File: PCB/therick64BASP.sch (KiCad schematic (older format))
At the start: 165 parts, among them J1 TYPE-C-31-M12_13, J2 AVR-ISP-6, K1 KEYSW, K10 KEYSW, K11 KEYSW, K12 KEYSW, K13 KEYSW, K14 KEYSW, K15 KEYSW, K16 KEYSW, K17 KEYSW, K18 KEYSW, K19 KEYSW, K2 KEYSW, K20 KEYSW, K21 KEYSW, K22 KEYSW, K23 KEYSW, K24 KEYSW, K25 KEYSW, K26 KEYSW, K27 KEYSW, K28 KEYSW, K29 KEYSW, K3 KEYSW, K30 KEYSW, K31 KEYSW, K32 KEYSW, K33 KEYSW, K34 KEYSW, K35 KEYSW, K36 KEYSW, K37 KEYSW, K38 KEYSW, K39 KEYSW, K4 KEYSW, K40 KEYSW, K41 KEYSW, K42 KEYSW, K43 KEYSW, K44 KEYSW, K45 KEYSW, K46 KEYSW, K47 KEYSW, K48 KEYSW, K49 KEYSW, K5 KEYSW, K50 KEYSW, K51 KEYSW, K52 KEYSW, K53 KEYSW, K54 KEYSW, K55 KEYSW, K56 KEYSW, K57 KEYSW, K58 KEYSW, K59 KEYSW, K6 KEYSW, K60 KEYSW, K61 KEYSW, K62 KEYSW, K63 KEYSW, K64 KEYSW, K7 KEYSW, K8 KEYSW, K9 KEYSW, SW1 SW_PUSH, U1 ATMEGA32U4, U2 HOLE, U3 USBLC6-2SC6, U4 HOLE, U5 HOLE, U6 HOLE, U7 HOLE, U8 HOLE, Y1 16MHz

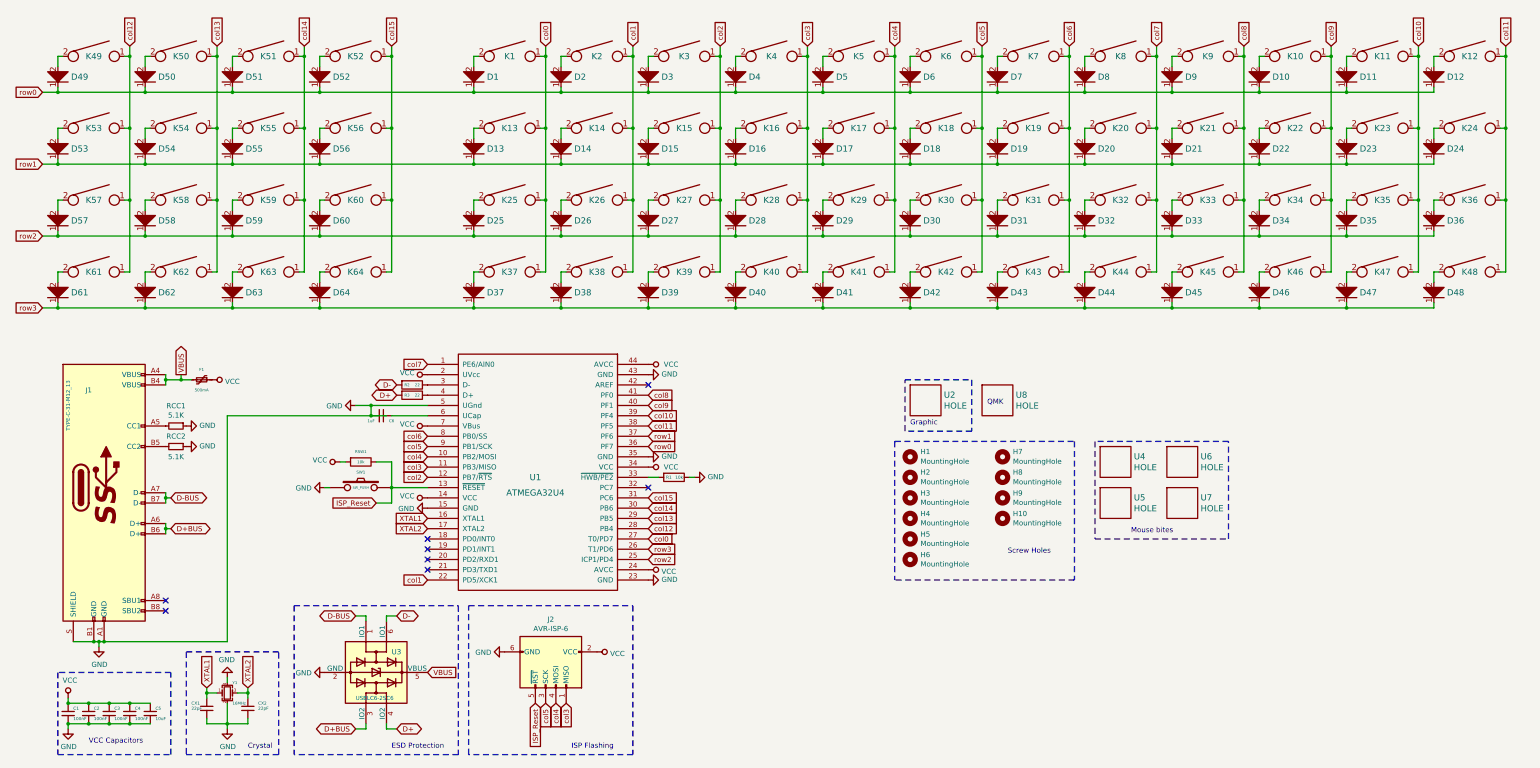
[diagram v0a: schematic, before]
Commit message: Changed pins to make routing cleaner
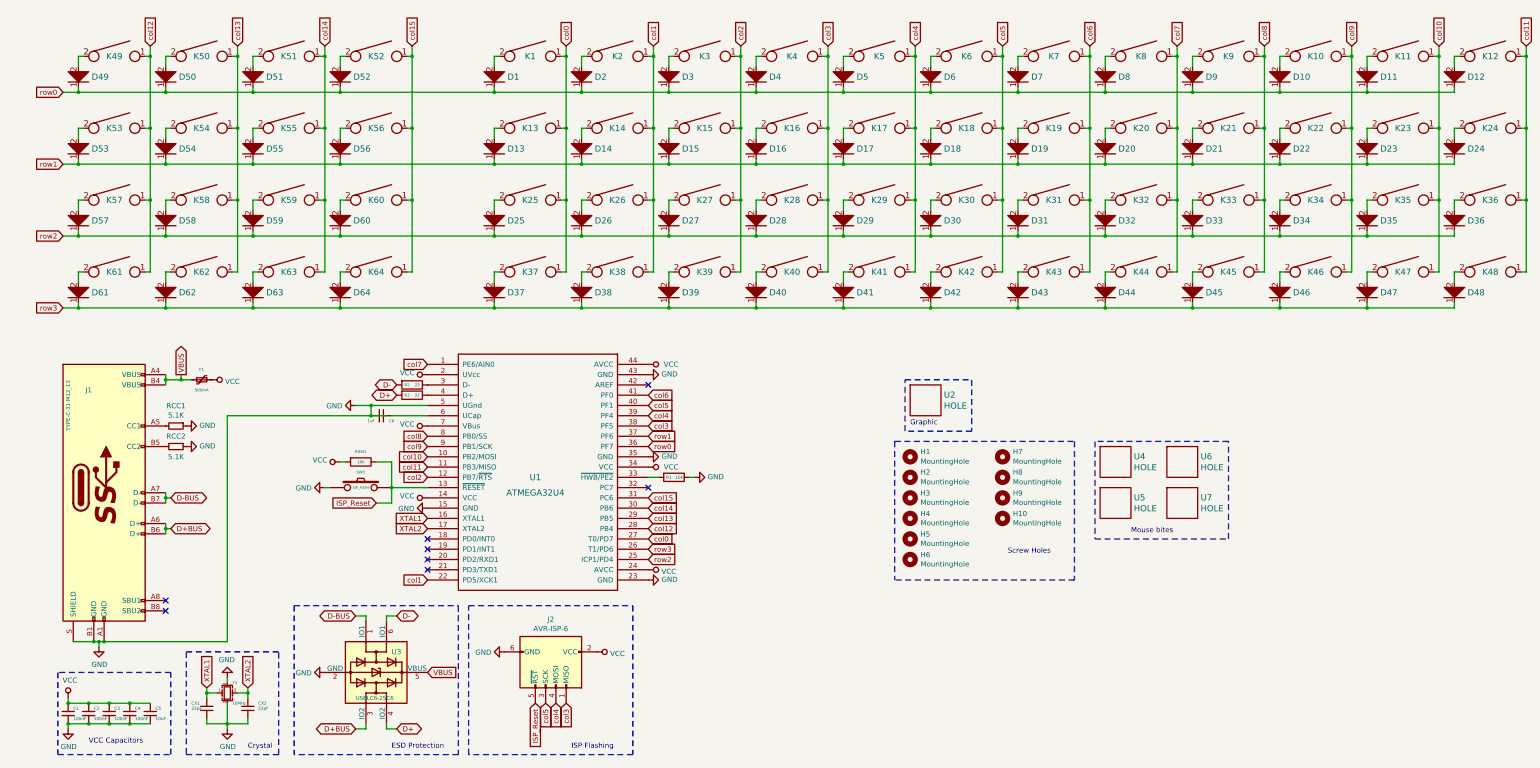
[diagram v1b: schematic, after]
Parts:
- removed U8: HOLE, Artwork:QMKBadgeSmall, symbol lets_split-cache:HOLE
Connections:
- net col10: now also U1.10 (PB2/MOSI); no longer U1.39 (PF4)
- net col11: now also U1.11 (PB3/MISO); no longer U1.38 (PF5)
- net col3: now also U1.38 (PF5); no longer U1.11 (PB3/MISO)
- net col4: now also U1.39 (PF4); no longer U1.10 (PB2/MOSI)
- net col5: now also U1.40 (PF1); no longer U1.9 (PB1/SCK)
- net col6: now also U1.41 (PF0); no longer U1.8 (PB0/SS)
- net col8: now also U1.8 (PB0/SS); no longer U1.41 (PF0)
- net col9: now also U1.9 (PB1/SCK); no longer U1.40 (PF1)
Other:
- note removed: "QMK"
- moved on the sheet: D1, D10, D11, D12, D13, D14, D15, D16, D17, D18, D19, D2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

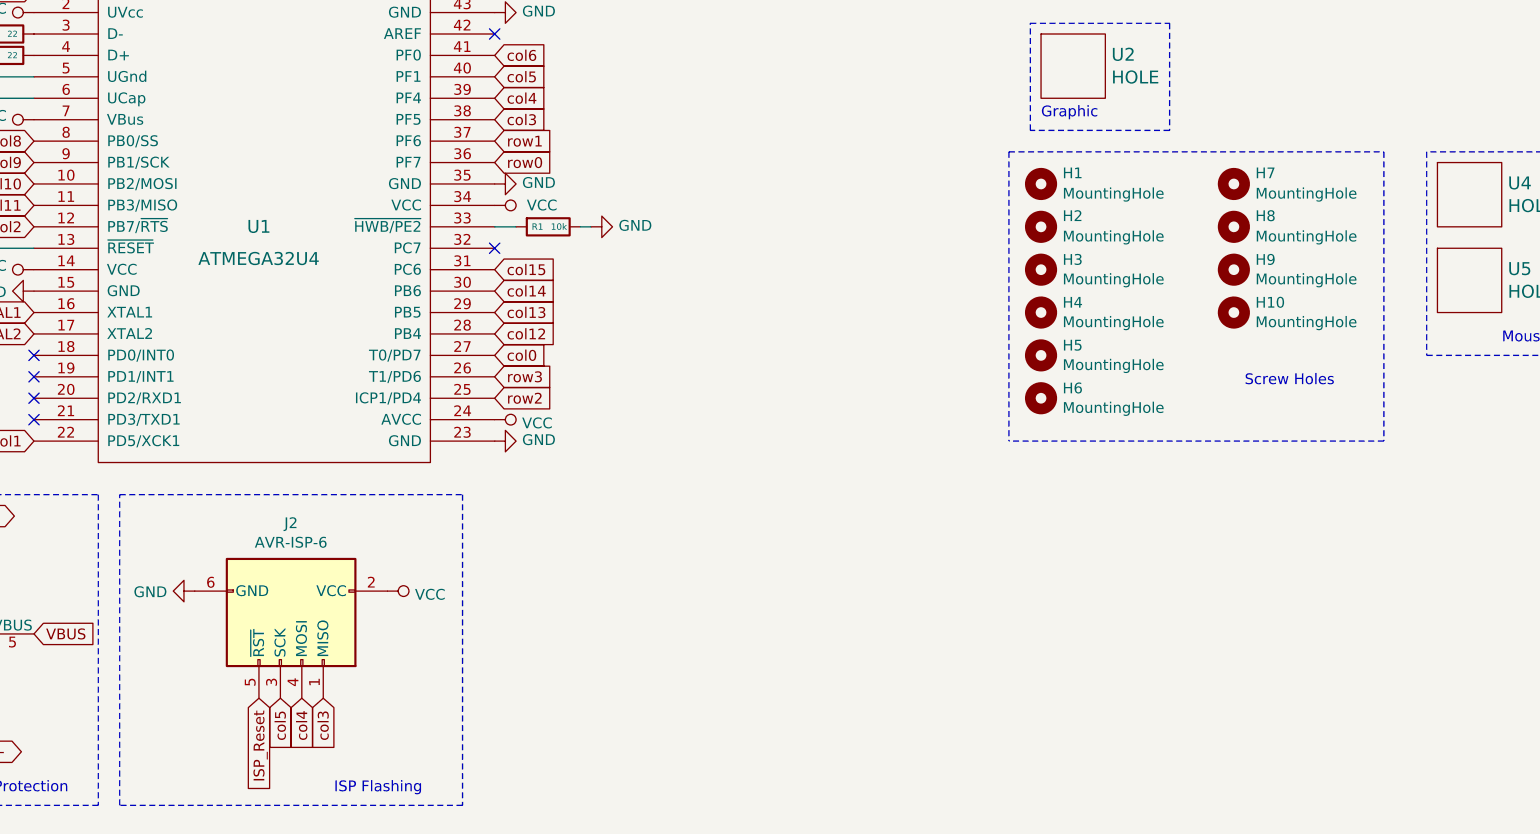
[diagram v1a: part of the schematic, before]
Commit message: Remapped ISP Flash, added mounting holes
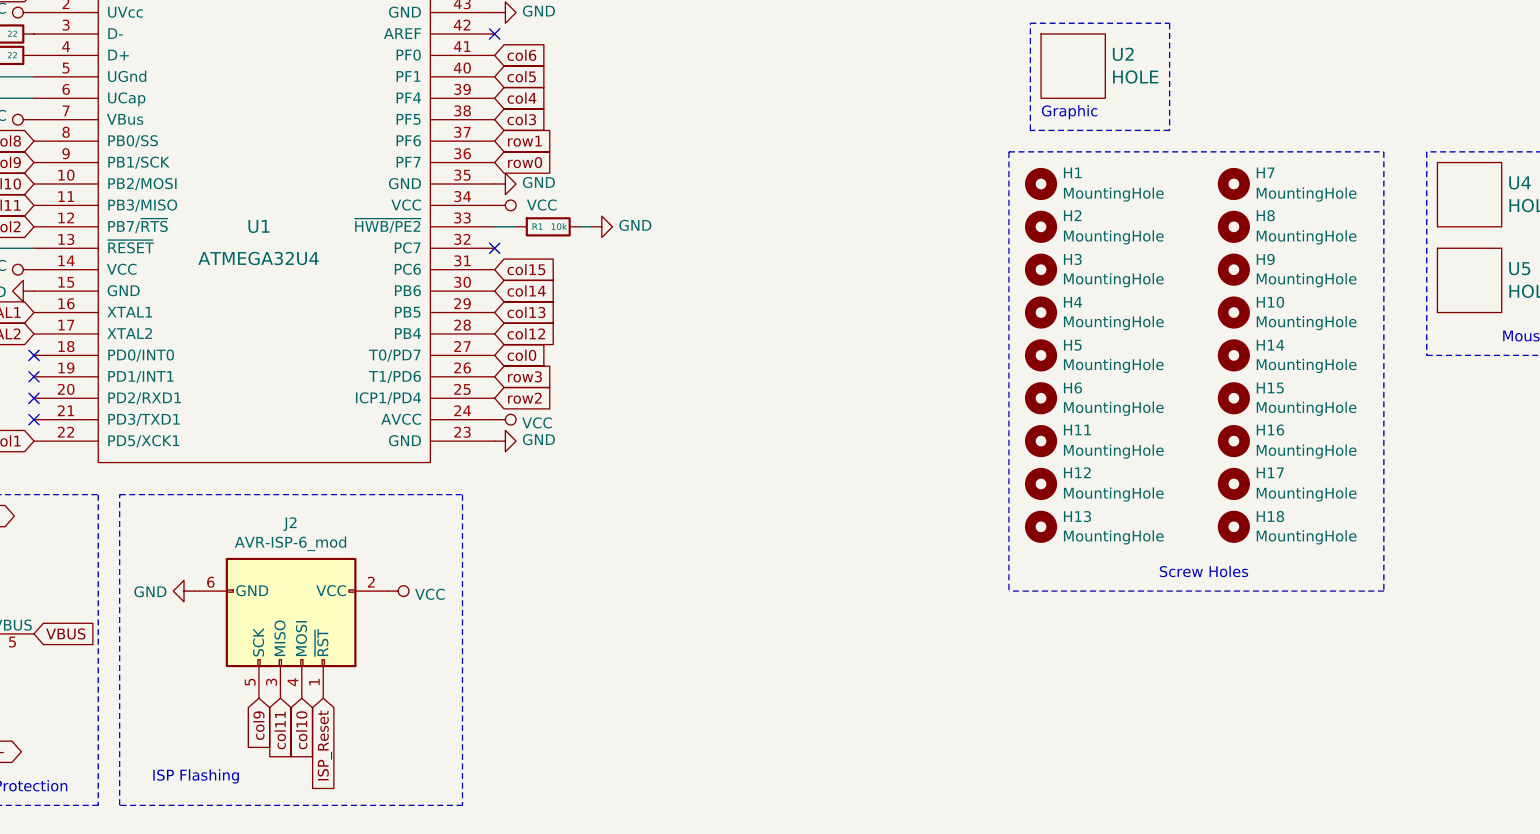
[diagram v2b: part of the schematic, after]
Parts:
- removed J2: AVR-ISP-6, Keeb_footprints:PIN_HEADER_1x6_OFFSET, symbol Connector:AVR-ISP-6
- added H11, H12, H13, H14, H15, H16, H17, H18: MountingHole, random-keyboard-parts:plate_hole_4mm_tht, symbol Mechanical:MountingHole
- added J2: AVR-ISP-6_mod, Keeb_footprints:PIN_HEADER_1x6_OFFSET, symbol Connector:AVR-ISP-6_mod
- H1, H10, H2, H3, H4, H5, H6, H7, H8, H9: footprint random-keyboard-parts:Generic-Mounthole -> random-keyboard-parts:plate_hole_4mm_tht
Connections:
- net GND: now also J2.6 (GND)
- net ISP_Reset: now also J2.1 (~RST)
- net VCC: now also J2.2 (VCC)
- net col10: now also J2.4 (MOSI)
- net col11: now also J2.3 (MISO)
- net col9: now also J2.5 (SCK)
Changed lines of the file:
@@
 F 0 "H1" H 9350 4850 50  0000 L CNN
 F 1 "MountingHole" H 9350 4755 50  0000 L CNN
-F 2 "random-keyboard-parts:Generic-Mounthole" H 9250 4800 50  0001 C CNN
+F 2 "random-keyboard-parts:plate_hole_4mm_tht" H 9250 4800 50  0001 C CNN
 F 3 "~" H 9250 4800 50  0001 C CNN
 	1    9250 4800
@@
 F 0 "H3" H 9350 5246 50  0000 L CNN
 F 1 "MountingHole" H 9350 5155 50  0000 L CNN
-F 2 "random-keyboard-parts:Generic-Mounthole" H 9250 5200 50  0001 C CNN
+F 2 "random-keyboard-parts:plate_hole_4mm_tht" H 9250 5200 50  0001 C CNN
 F 3 "~" H 9250 5200 50  0001 C CNN
 	1    9250 5200
@@
 F 0 "H4" H 9350 5446 50  0000 L CNN
 F 1 "MountingHole" H 9350 5355 50  0000 L CNN
-F 2 "random-keyboard-parts:Generic-Mounthole" H 9250 5400 50  0001 C CNN
+F 2 "random-keyboard-parts:plate_hole_4mm_tht" H 9250 5400 50  0001 C CNN
 F 3 "~" H 9250 5400 50  0001 C CNN
 	1    9250 5400
@@
 F 0 "H5" H 9350 5646 50  0000 L CNN
 F 1 "MountingHole" H 9350 5555 50  0000 L CNN
-F 2 "random-keyboard-parts:Generic-Mounthole" H 9250 5600 50  0001 C CNN
+F 2 "random-keyboard-parts:plate_hole_4mm_tht" H 9250 5600 50  0001 C CNN
 F 3 "~" H 9250 5600 50  0001 C CNN
 	1    9250 5600
@@
 F 0 "H6" H 9350 5846 50  0000 L CNN
 F 1 "MountingHole" H 9350 5755 50  0000 L CNN
-F 2 "random-keyboard-parts:Generic-Mounthole" H 9250 5800 50  0001 C CNN
+F 2 "random-keyboard-parts:plate_hole_4mm_tht" H 9250 5800 50  0001 C CNN
 F 3 "~" H 9250 5800 50  0001 C CNN
 	1    9250 5800
@@
 Wire Notes Line
 	2050 6900 950  6900
-Text Notes 10200 5750 0    50   ~ 0
+Text Notes 9800 6650 0    50   ~ 0
 Screw Holes
 Text Notes 9250 4500 0    50   ~ 0
@@
 F 0 "H2" H 9350 5050 50  0000 L CNN
 F 1 "MountingHole" H 9350 4955 50  0000 L CNN
-F 2 "random-keyboard-parts:Generic-Mounthole" H 9250 5000 50  0001 C CNN
+F 2 "random-keyboard-parts:plate_hole_4mm_tht" H 9250 5000 50  0001 C CNN
 F 3 "~" H 9250 5000 50  0001 C CNN
 	1    9250 5000
@@
 	0    1    1    0
 $EndComp
-$Comp
-L Connector:AVR-ISP-6 J2
-U 1 1 5E280E11
-P 5700 6800
-F 0 "J2" V 5283 6850 50  0000 C CNN
-F 1 "AVR-ISP-6" V 5374 6850 50  0000 C CNN
-F 2 "Keeb_footprints:PIN_HEADER_1x6_OFFSET" V 5450 6850 50  0001 C CNN
-F 3 " ~" H 4425 6250 50  0001 C CNN
-	1    5700 6800
-	0    1    1    0
-$EndComp
 Text GLabel 5800 7200 3    50   Input ~ 0
-col4
-Text GLabel 5900 7200 3    50   Input ~ 0
-col3
+col10
+Text GLabel 5600 7200 3    50   Input ~ 0
+col9
 Text GLabel 5700 7200 3    50   Input ~ 0
-col5
+col11
 $Comp
 L power:GND #PWR0121
@@
 Text GLabel 4050 5250 0    50   Input ~ 0
 ISP_Reset
-Text GLabel 5600 7200 3    50   Input ~ 0
+Text GLabel 5900 7200 3    50   Input ~ 0
 ISP_Reset
-Text Notes 5950 7650 0    50   ~ 0
+Text Notes 5100 7600 0    50   ~ 0
 ISP Flashing
 Wire Notes Line
@@
 F 0 "H7" H 10250 4850 50  0000 L CNN
 F 1 "MountingHole" H 10250 4755 50  0000 L CNN
-F 2 "random-keyboard-parts:Generic-Mounthole" H 10150 4800 50  0001 C CNN
+F 2 "random-keyboard-parts:plate_hole_4mm_tht" H 10150 4800 50  0001 C CNN
 F 3 "~" H 10150 4800 50  0001 C CNN
 	1    10150 4800
@@
 F 0 "H9" H 10250 5246 50  0000 L CNN
 F 1 "MountingHole" H 10250 5155 50  0000 L CNN
-F 2 "random-keyboard-parts:Generic-Mounthole" H 10150 5200 50  0001 C CNN
+F 2 "random-keyboard-parts:plate_hole_4mm_tht" H 10150 5200 50  0001 C CNN
 F 3 "~" H 10150 5200 50  0001 C CNN
 	1    10150 5200
@@
 F 0 "H10" H 10250 5446 50  0000 L CNN
 F 1 "MountingHole" H 10250 5355 50  0000 L CNN
-F 2 "random-keyboard-parts:Generic-Mounthole" H 10150 5400 50  0001 C CNN
+F 2 "random-keyboard-parts:plate_hole_4mm_tht" H 10150 5400 50  0001 C CNN
 F 3 "~" H 10150 5400 50  0001 C CNN
 	1    10150 5400
@@
 F 0 "H8" H 10250 5050 50  0000 L CNN
 F 1 "MountingHole" H 10250 4955 50  0000 L CNN
-F 2 "random-keyboard-parts:Generic-Mounthole" H 10150 5000 50  0001 C CNN
+F 2 "random-keyboard-parts:plate_hole_4mm_tht" H 10150 5000 50  0001 C CNN
 F 3 "~" H 10150 5000 50  0001 C CNN
 	1    10150 5000
@@
 Wire Notes Line
 	9100 4650 10850 4650
-Wire Notes Line
-	10850 4650 10850 6000
-Wire Notes Line
-	10850 6000 9100 6000
-Wire Notes Line
-	9100 4650 9100 6000
 Text Notes 11400 5550 0    50   ~ 0
 Mouse bites
@@
 Connection ~ 3700 3350
 Connection ~ 5200 3350
+$Comp
+L Connector:AVR-ISP-6_mod J2
+U 1 1 5EC10E7A
+P 5700 6800
+F 0 "J2" V 5283 6850 50  0000 C CNN
+F 1 "AVR-ISP-6_mod" V 5374 6850 50  0000 C CNN
+F 2 "Keeb_footprints:PIN_HEADER_1x6_OFFSET" V 5450 6850 50  0001 C CNN
+F 3 " ~" H 4425 6250 50  0001 C CNN
+	1    5700 6800
+	0    1    1    0
+$EndComp
+$Comp
+L Mechanical:MountingHole H11
+U 1 1 5EC1BF71
+P 9250 6000
+F 0 "H11" H 9350 6050 50  0000 L CNN
+F 1 "MountingHole" H 9350 5955 50  0000 L CNN
+F 2 "random-keyboard-parts:plate_hole_4mm_tht" H 9250 6000 50  0001 C CNN
+F 3 "~" H 9250 6000 50  0001 C CNN
+	1    9250 6000
+	1    0    0    -1
+$EndComp
+$Comp
+L Mechanical:MountingHole H13
+U 1 1 5EC1BF77
+P 9250 6400
+F 0 "H13" H 9350 6446 50  0000 L CNN
+F 1 "MountingHole" H 9350 6355 50  0000 L CNN
+F 2 "random-keyboard-parts:plate_hole_4mm_tht" H 9250 6400 50  0001 C CNN
+F 3 "~" H 9250 6400 50  0001 C CNN
+	1    9250 6400
+	1    0    0    -1
+$EndComp
+$Comp
+L Mechanical:MountingHole H14
+U 1 1 5EC1BF7D
+P 10150 5600
+F 0 "H14" H 10250 5646 50  0000 L CNN
+F 1 "MountingHole" H 10250 5555 50  0000 L CNN
+F 2 "random-keyboard-parts:plate_hole_4mm_tht" H 10150 5600 50  0001 C CNN
+F 3 "~" H 10150 5600 50  0001 C CNN
+	1    10150 5600
+	1    0    0    -1
+$EndComp
+$Comp
+L Mechanical:MountingHole H12
+U 1 1 5EC1BF83
+P 9250 6200
+F 0 "H12" H 9350 6250 50  0000 L CNN
+F 1 "MountingHole" H 9350 6155 50  0000 L CNN
+F 2 "random-keyboard-parts:plate_hole_4mm_tht" H 9250 6200 50  0001 C CNN
+F 3 "~" H 9250 6200 50  0001 C CNN
+	1    9250 6200
+	1    0    0    -1
+$EndComp
+$Comp
+L Mechanical:MountingHole H16
+U 1 1 5EC1BF89
+P 10150 6000
+F 0 "H16" H 10250 6050 50  0000 L CNN
+F 1 "MountingHole" H 10250 5955 50  0000 L CNN
+F 2 "random-keyboard-parts:plate_hole_4mm_tht" H 10150 6000 50  0001 C CNN
+F 3 "~" H 10150 6000 50  0001 C CNN
+	1    10150 6000
+	1    0    0    -1
+$EndComp
+$Comp
+L Mechanical:MountingHole H18
+U 1 1 5EC1BF8F
+P 10150 6400
+F 0 "H18" H 10250 6446 50  0000 L CNN
+F 1 "MountingHole" H 10250 6355 50  0000 L CNN
+F 2 "random-keyboard-parts:plate_hole_4mm_tht" H 10150 6400 50  0001 C CNN
+F 3 "~" H 10150 6400 50  0001 C CNN
+	1    10150 6400
+	1    0    0    -1
+$EndComp
+$Comp
+L Mechanical:MountingHole H15
+U 1 1 5EC1BF95
+P 10150 5800
+F 0 "H15" H 10250 5846 50  0000 L CNN
+F 1 "MountingHole" H 10250 5755 50  0000 L CNN
+F 2 "random-keyboard-parts:plate_hole_4mm_tht" H 10150 5800 50  0001 C CNN
+F 3 "~" H 10150 5800 50  0001 C CNN
+	1    10150 5800
+	1    0    0    -1
+$EndComp
+$Comp
+L Mechanical:MountingHole H17
+U 1 1 5EC1BF9B
+P 10150 6200
+F 0 "H17" H 10250 6250 50  0000 L CNN
+F 1 "MountingHole" H 10250 6155 50  0000 L CNN
+F 2 "random-keyboard-parts:plate_hole_4mm_tht" H 10150 6200 50  0001 C CNN
+F 3 "~" H 10150 6200 50  0001 C CNN
+	1    10150 6200
+	1    0    0    -1
+$EndComp
+Wire Notes Line
+	10850 4650 10850 6700
+Wire Notes Line
+	10850 6700 9100 6700
+Wire Notes Line
+	9100 4650 9100 6700
 $EndSCHEMATC
